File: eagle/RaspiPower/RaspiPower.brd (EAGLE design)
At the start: 50 x 50 mm, 22 parts, among them J3 455-1750-1-ND, J4 455-1750-1-ND, J5 AVR_SPI_PROG_3X2PTH, K1 4052

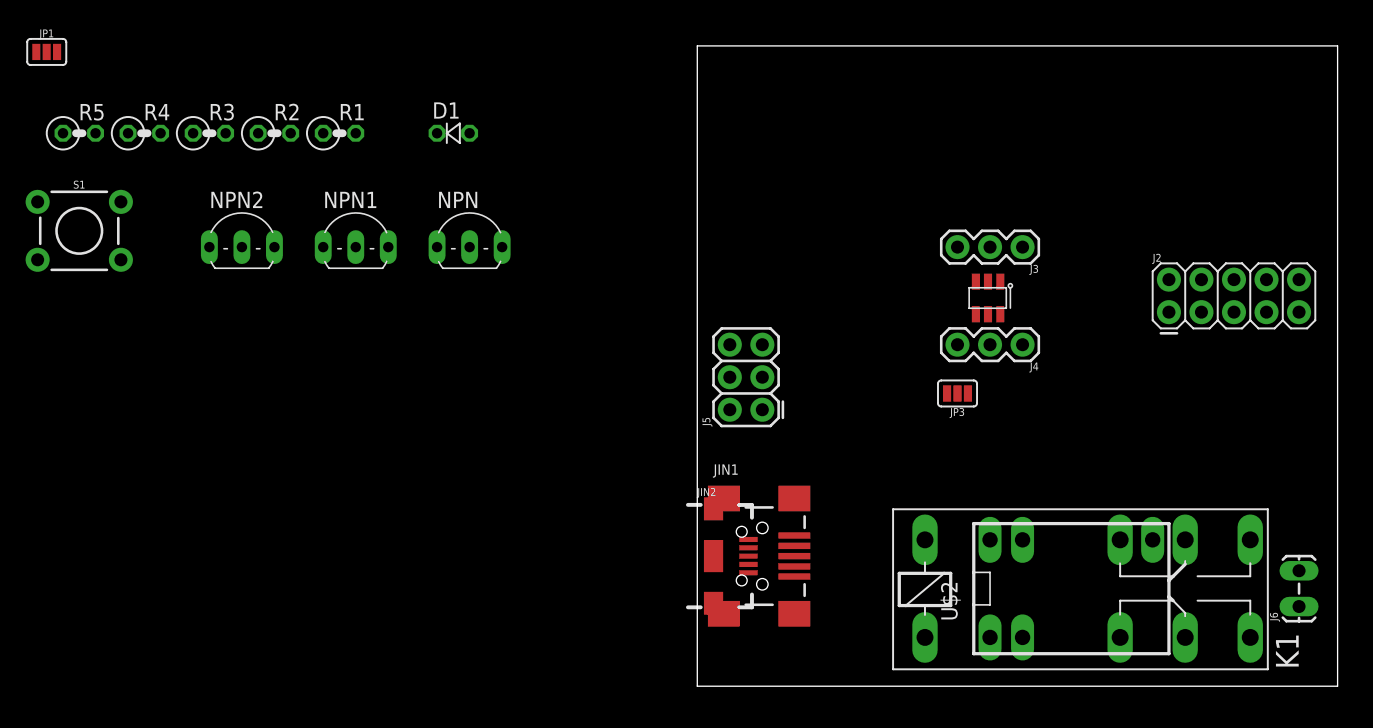
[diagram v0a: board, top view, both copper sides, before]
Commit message: Draft placement, now on to the routing
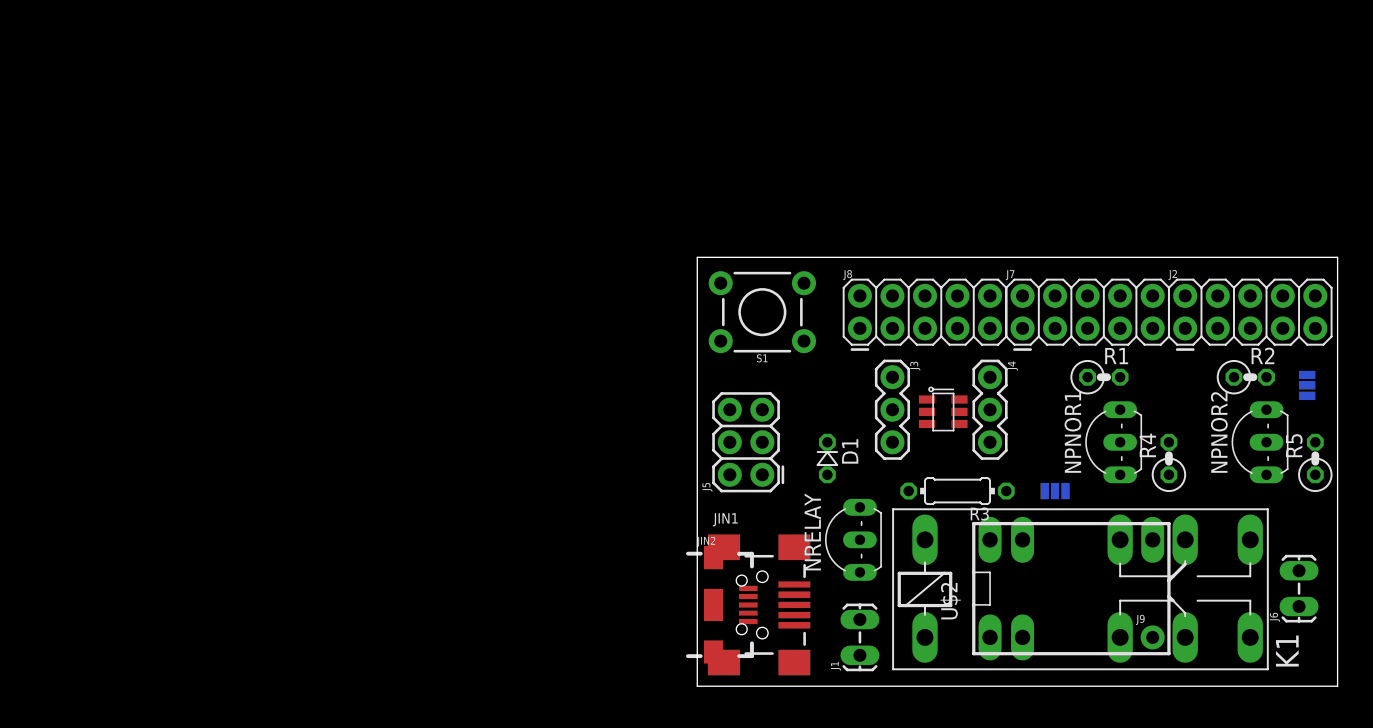
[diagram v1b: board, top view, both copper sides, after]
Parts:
- removed NPN, NPN1, NPN2: 2SC2120, transistor:TO92-ECB
- added J1: (no value), SparkFun-Connectors:1X02_LOCK_LONGPADS
- added J7, J8: (no value), SparkFun-Connectors:2X5
- added J9: (no value), SparkFun-Connectors:1X01_NO_SILK
- added NPNOR1, NPNOR2, NRELAY: 2SC2120, transistor:TO92-ECB
- J3, J4: value 455-1750-1-ND -> (none)
- JP1, JP3: value JUMPER-SMT_3_NO_SILK -> (none)
- R3: device resistor:0207/2V -> resistor:0204/7
- moved JP1 101.8 mm to (47.6, 23.5), flipped to the bottom, turned to 270 degrees
- moved R5 99.8 mm to (48.3, 17.8), turned to 90 degrees
- moved R4 83.9 mm to (36.8, 17.8), turned to 90 degrees
- moved R2 78.5 mm to (43.2, 24.1)
- moved R3 64.8 mm to (20.3, 15.2), turned to 180 degrees
- moved R1 62.7 mm to (31.8, 24.1)
- moved S1 53.7 mm to (5.08, 29.2), turned to 180 degrees
- moved D1 38.7 mm to (10.2, 17.8), turned to 270 degrees
- moved J3 14.4 mm to (15.2, 24.1), turned to 270 degrees
- moved JP3 10.8 mm to (27.9, 15.2), flipped to the bottom, turned to 0 degrees
- moved U$1 10.0 mm to (18.4, 22.9), turned to 270 degrees
- moved J5 5.08 mm to (5.08, 16.5)
- moved JIN1 3.81 mm to (5.08, 6.35)
- moved JIN2 3.81 mm to (1.27, 6.35)
- moved J4 3.59 mm to (22.9, 24.1), turned to 270 degrees
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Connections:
- net GND: now also J1.1, NRELAY.E; no longer NPN.E
- net N$11: now also NPNOR1.B; no longer NPN1.B
- net N$12: now also NPNOR2.B; no longer NPN2.B
- net N$4: now also NPNOR1.E, NPNOR2.E; no longer NPN1.E, NPN2.E
- net N$8: now also NRELAY.B; no longer NPN.B
- net N$9: now also NRELAY.C; no longer NPN.C
- net VCC: now also J1.2, NPNOR1.C, NPNOR2.C; no longer NPN1.C, NPN2.C
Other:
- board size 50 x 50 mm -> 50 x 33.5 mm

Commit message: Last changes before routing, added power LED
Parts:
- added J10: (no value), SparkFun-Connectors:1X01_NO_SILK
- added JOUT: (no value), SparkFun-Connectors:1X02_LOCK_LONGPADS
- added LED_POWER2: (no value), SparkFun-LED:FKIT-LED-1206
- added R6: 1k, resistor:R1206W
- D1: device diode:D-2.5 -> diode:D-5
- J6: device SparkFun-Connectors:1X02_LOCK_LONGPADS -> SparkFun-Connectors:1X01_NO_SILK
- R4, R5: value 1k -> 10k
- moved JP1 28.0 mm to (19.7, 25.4)
- moved R5 20.5 mm to (29.2, 25.4), turned to 0 degrees
- moved R1 5.39 mm to (27.9, 20.3), turned to 90 degrees
- moved J6 1.59 mm to (48.6, 6.35), turned to 0 degrees
- moved D1 1.42 mm to (9.53, 16.5)
- moved J2 0.63 mm to (38.1, 28.6)
- moved J7 0.63 mm to (25.4, 28.6)
- moved J8 0.63 mm to (12.7, 28.6)
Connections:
- new net N$1: LED_POWER2.A, R6.1
- net GND: now also JOUT.2, LED_POWER2.C; no longer J6.2
- net N$3: now also JOUT.1; no longer J6.1
- net VCC: now also R6.2
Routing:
- added copper zone on layer 16, net GND
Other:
- board text added: "E C B"

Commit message: switched pins of tact switch for easier routing
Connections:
- net CLK-BUTTON: now also S1.1; no longer S1.3
- net GND: now also S1.3; no longer S1.1
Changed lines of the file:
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@@
 <autorouter>
 <pass name="Default">
-<param name="RoutingGrid" value="50mil"/>
+<param name="RoutingGrid" value="0.125mm"/>
 <param name="AutoGrid" value="1"/>
-<param name="Efforts" value="0"/>
+<param name="Efforts" value="1"/>
 <param name="TopRouterVariant" value="1"/>
 <param name="tpViaShape" value="round"/>
-<param name="PrefDir.1" value="a"/>
+<param name="PrefDir.1" value="*"/>
 <param name="PrefDir.2" value="0"/>
 <param name="PrefDir.3" value="0"/>
@@
 <param name="PrefDir.14" value="0"/>
 <param name="PrefDir.15" value="0"/>
-<param name="PrefDir.16" value="a"/>
+<param name="PrefDir.16" value="*"/>
 <param name="cfVia" value="8"/>
 <param name="cfNonPref" value="5"/>
@@
 <element name="R4" library="resistor" package="0207/2V" value="10k" x="36.83" y="17.78" rot="R90"/>
 <element name="R5" library="resistor" package="0207/2V" value="10k" x="29.21" y="25.4"/>
-<element name="S1" library="SparkFun-Switches" package="TACTILE_SWITCH_PTH_6.0MM" value="MOMENTARY-SWITCH-SPST-PTH-6.0MM" x="5.08" y="29.21" rot="R180">
-<attribute name="SF_SKU" value="COM-00097" x="5.08" y="29.21" size="1.778" layer="27" rot="R180" display="off"/>
-<attribute name="PROD_ID" value=" SWCH-08441" x="5.08" y="29.21" size="1.778" layer="27" rot="R180" display="off"/>
-</element>
 <element name="U$1" library="kalshagar" package="SOT23" value="ATTINY10" x="18.415" y="22.86" rot="R270"/>
 <element name="J2" library="SparkFun-Connectors" package="2X5" value="" x="38.1" y="28.575">
@@
 <element name="J6" library="SparkFun-Connectors" package="1X01_NO_SILK" value="" x="48.5775" y="6.35"/>
 <element name="J10" library="SparkFun-Connectors" package="1X01_NO_SILK" value="" x="48.5775" y="13.97"/>
+<element name="S1" library="SparkFun-Switches" package="TACTILE_SWITCH_PTH_6.0MM" value="MOMENTARY-SWITCH-SPST-PTH-6.0MM" x="5.08" y="29.21" rot="R180">
+<attribute name="SF_SKU" value="COM-00097" x="5.08" y="29.21" size="1.778" layer="27" rot="R180" display="off"/>
+<attribute name="PROD_ID" value=" SWCH-08441" x="5.08" y="29.21" size="1.778" layer="27" rot="R180" display="off"/>
+</element>
 </elements>
 <signals>
@@
 <contactref element="U$1" pad="P$2"/>
 <contactref element="J3" pad="2"/>
-<contactref element="S1" pad="1"/>
 <contactref element="NRELAY" pad="E"/>
 <contactref element="R4" pad="1"/>
@@
 </polygon>
 <contactref element="LED_POWER2" pad="C"/>
+<contactref element="S1" pad="3"/>
 <wire x1="46.355" y1="11.557" x2="47.9425" y2="22.708" width="0" layer="19" extent="1-1"/>
 <wire x1="17.93875" y1="21.43125" x2="15.24" y2="21.59" width="0" layer="19" extent="1-1"/>
@@
 <contactref element="U$1" pad="P$3"/>
 <contactref element="J3" pad="3"/>
-<contactref element="S1" pad="3"/>
 <contactref element="J5" pad="3"/>
+<contactref element="S1" pad="1"/>
 <wire x1="15.24" y1="19.05" x2="17.93875" y2="20.47875" width="0" layer="19" extent="1-1"/>
 <wire x1="5.08" y1="19.05" x2="15.24" y2="19.05" width="0" layer="19" extent="1-1"/>
-<wire x1="8.3312" y1="31.4706" x2="5.08" y2="19.05" width="0" layer="19" extent="1-1"/>
+<wire x1="8.3312" y1="26.9494" x2="5.08" y2="19.05" width="0" layer="19" extent="1-1"/>
 </signal>
 <signal name="N$5">

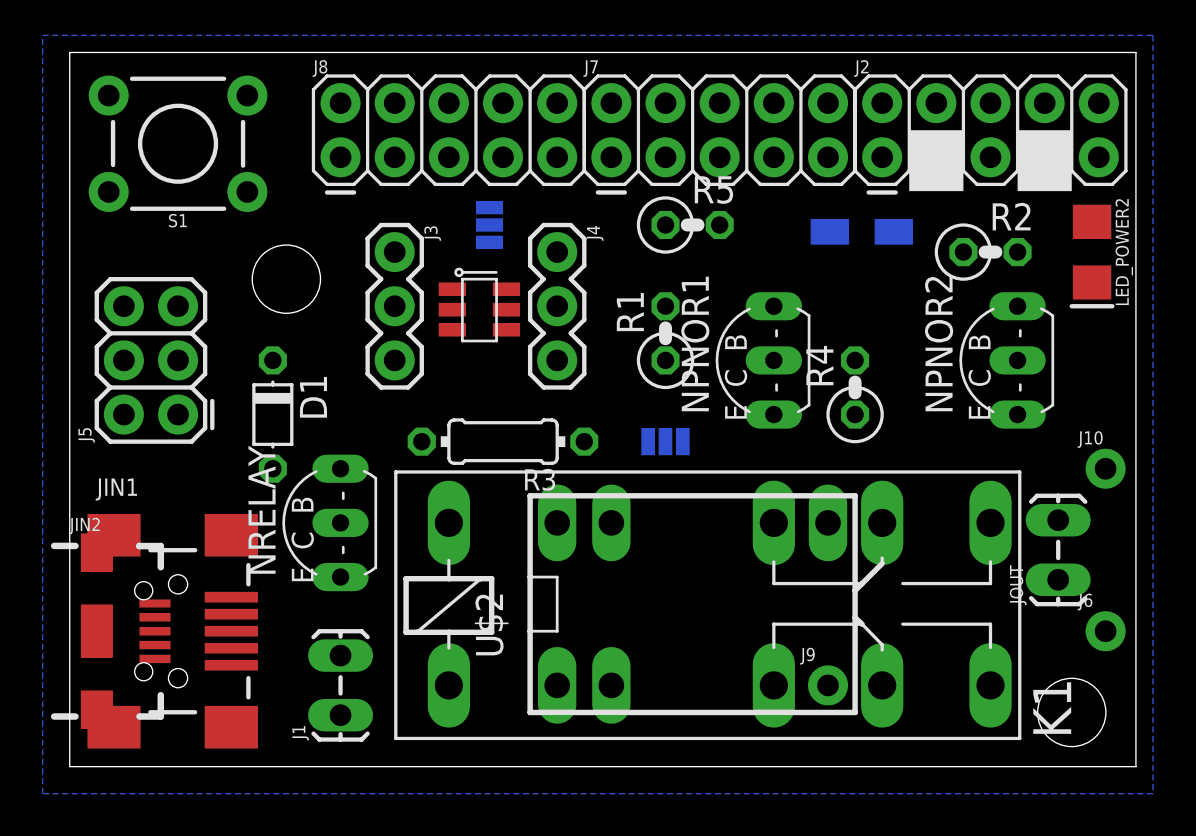
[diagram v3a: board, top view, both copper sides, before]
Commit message: Routing looks ok, now todo final review and board silk
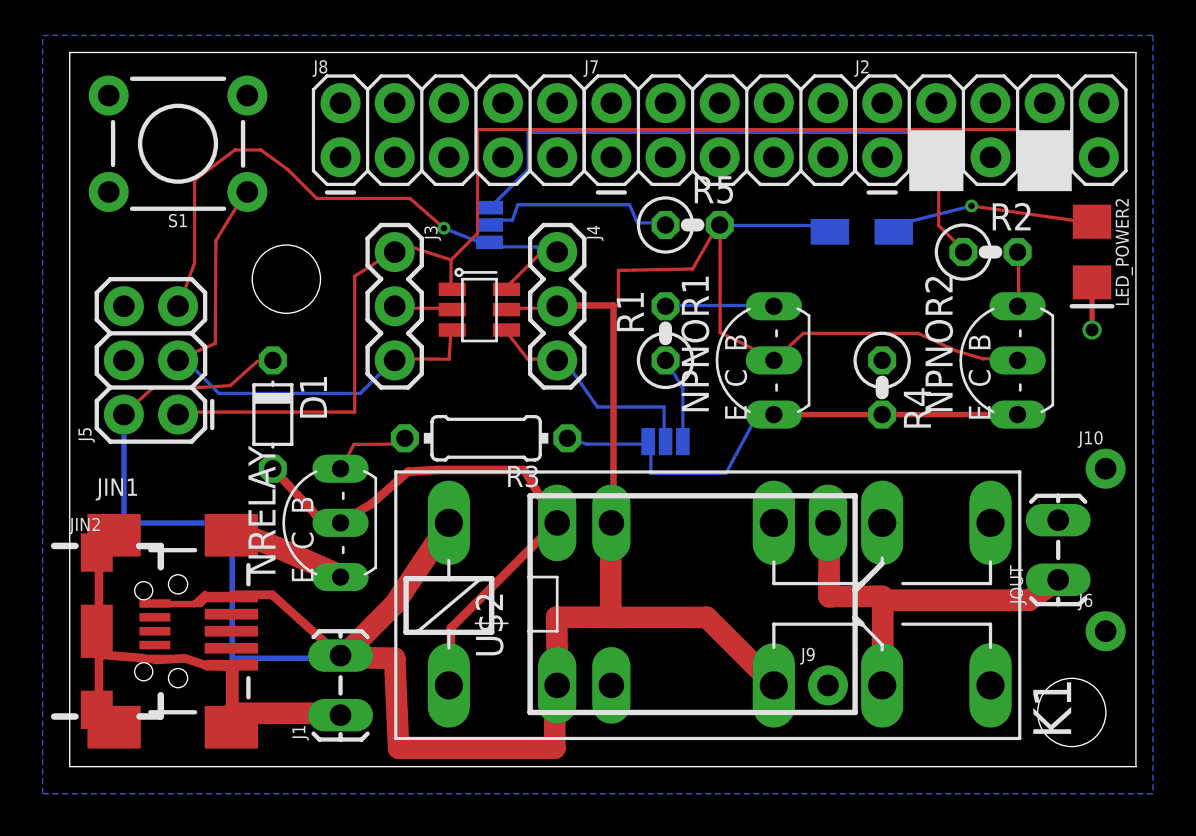
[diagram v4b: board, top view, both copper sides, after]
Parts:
- moved R4 1.27 mm to (38.1, 17.8), turned to 270 degrees
- moved R3 0.81 mm to (19.5, 15.4)
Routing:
- net VCC: track 0.00 -> 135.7 mm
- net DATA-DOSHUTDN: track 0.00 -> 55.1 mm
- net GND: track 0.00 -> 37.0 mm, vias 0 -> 1
- net PI_IS_ON: track 0.00 -> 28.9 mm
- net RESET: track 0.00 -> 28.4 mm, vias 0 -> 1
- net N$9: track 0.00 -> 26.3 mm
- net CLK-BUTTON: track 0.00 -> 24.9 mm
- net N$4: track 0.00 -> 24.3 mm
- net N$3: track 0.00 -> 18.7 mm
- net N$5: track 0.00 -> 11.0 mm
- net N$1: track 0.00 -> 9.63 mm, vias 0 -> 1
- net N$10: track 0.00 -> 9.49 mm
- net N$11: track 0.00 -> 5.11 mm
- net N$14: track 0.00 -> 4.04 mm
- net N$8: track 0.00 -> 3.77 mm
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
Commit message: Few changes, board in version 1.0 for prod
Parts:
- added C1: 10uF, resistor:E2,5-5
- moved R6 0.81 mm to (36.7, 25.8)
- turned JP1 to 90 degrees
- renumbered J1 to JIN, J5 to JSPIPROG
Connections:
- removed net N$10: JP1.2, R5.1
- new net N$7: JP1.1, R5.1
- net GND: now also C1.-
- net PI_IS_ON: now also JP1.3; no longer JP1.1
- net RESET: now also JP1.2; no longer JP1.3
- net VCC: now also C1.+
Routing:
- net N$7: track 0.00 -> 9.97 mm
- net N$10: track 9.49 -> 0.00 mm
- net VCC: track 135.7 -> 142.0 mm
- net N$2: track 0.00 -> 2.17 mm
- net PI_IS_ON: track 28.9 -> 29.7 mm
- net RESET: track 28.4 -> 28.2 mm, vias 1 -> 0
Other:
- board text added: "+"
- board text added: "-"
- board text added: "A"
- board text added: "B"
- board text added: "HK4100F"
- board text added: "Raspi pin 40"
- board text added: "RaspiPower"
- board text added: "Tiny10"
- board text added: "electrogeek.cc/RaspiPower"
- board text added: "v1.0 - Sept 2017"
